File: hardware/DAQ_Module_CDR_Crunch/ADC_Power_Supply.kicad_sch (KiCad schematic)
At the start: 12 parts, among them U5 TPS70933DBVR, U6 TPS70933DBVR

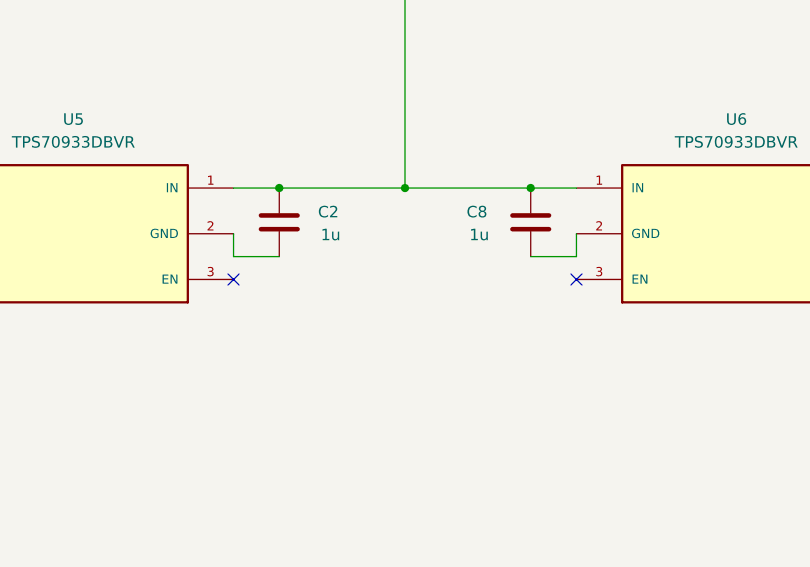
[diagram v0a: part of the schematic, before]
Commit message: Ready for final review. Added downloadable footprint and symbol of board
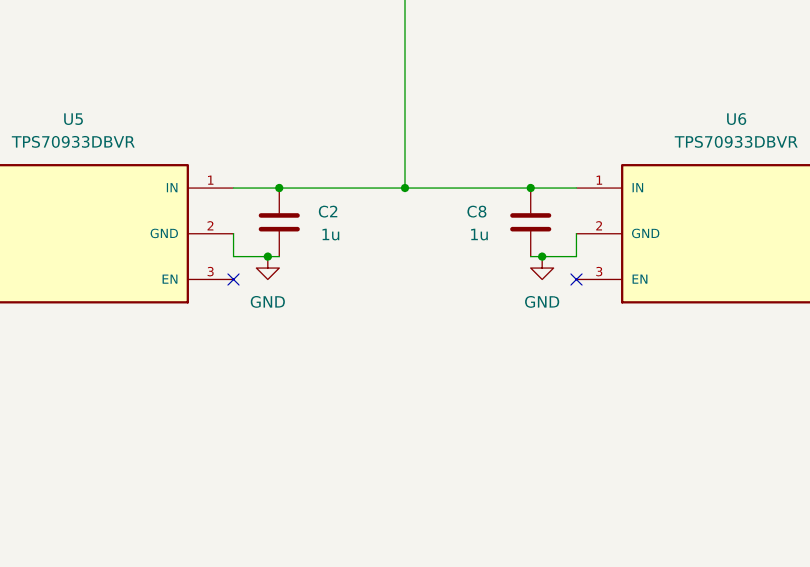
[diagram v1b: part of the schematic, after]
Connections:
- net GND: now also C2.1, C8.2, U5.2 (GND), U6.2 (GND)
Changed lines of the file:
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@@
+	)
+	(junction
+		(at 137.16 80.01)
+		(diameter 0)
+		(color 0 0 0 0)
 	)
 	(junction
@@
 	)
 	(junction
+		(at 106.68 80.01)
+		(diameter 0)
+		(color 0 0 0 0)
+	)
+	(junction
 		(at 195.58 105.41)
 		(diameter 0)
@@
 	(wire
 		(pts
-			(xy 107.95 80.01) (xy 102.87 80.01)
+			(xy 107.95 80.01) (xy 106.68 80.01)
 		)
 		(stroke
@@
 	(wire
 		(pts
-			(xy 135.89 80.01) (xy 140.97 80.01)
+			(xy 135.89 80.01) (xy 137.16 80.01)
+		)
+		(stroke
+			(width 0)
+			(type default)
+		)
+	)
+	(wire
+		(pts
+			(xy 106.68 80.01) (xy 102.87 80.01)
 		)
 		(stroke
@@
 		(pts
 			(xy 195.58 105.41) (xy 190.5 105.41)
+		)
+		(stroke
+			(width 0)
+			(type default)
+		)
+	)
+	(wire
+		(pts
+			(xy 137.16 80.01) (xy 140.97 80.01)
 		)
 		(stroke
@@
 				(path "/5227b8b5-3dda-44a0-8387-0a3150b59ce6/912d4027-c9f3-433b-9488-65ed5c4fb033"
 					(reference "#PWR010")
+					(unit 1)
+				)
+			)
+		)
+	)
+	(symbol
+		(lib_id "power:GND")
+		(at 106.68 80.01 0)
+		(unit 1)
+		(exclude_from_sim no)
+		(in_bom yes)
+		(on_board yes)
+		(dnp no)
+		(fields_autoplaced yes)
+		(property "Reference" "#PWR02"
+			(at 106.68 86.36 0)
+			(effects
+				(font
+					(size 1.27 1.27)
+				)
+				(hide yes)
+			)
+		)
+		(property "Value" "GND"
+			(at 106.68 85.09 0)
+			(effects
+				(font
+					(size 1.27 1.27)
+				)
+			)
+		)
+		(property "Footprint" ""
+			(at 106.68 80.01 0)
+			(effects
+				(font
+					(size 1.27 1.27)
+				)
+				(hide yes)
+			)
+		)
+		(property "Datasheet" ""
+			(at 106.68 80.01 0)
+			(effects
+				(font
+					(size 1.27 1.27)
+				)
+				(hide yes)
+			)
+		)
+		(property "Description" "Power symbol creates a global label with name \"GND\" , ground"
+			(at 106.68 80.01 0)
+			(effects
+				(font
+					(size 1.27 1.27)
+				)
+				(hide yes)
+			)
+		)
+		(pin "1"
+		)
+		(instances
+			(project ""
+				(path "/5227b8b5-3dda-44a0-8387-0a3150b59ce6/912d4027-c9f3-433b-9488-65ed5c4fb033"
+					(reference "#PWR02")
 					(unit 1)
 				)
@@
 					(unit 1)
 				)
+			)
+		)
+	)
+	(symbol
+		(lib_id "power:GND")
+		(at 137.16 80.01 0)
+		(unit 1)
+		(exclude_from_sim no)
+		(in_bom yes)
+		(on_board yes)
+		(dnp no)
+		(fields_autoplaced yes)
+		(property "Reference" "#PWR06"
+			(at 137.16 86.36 0)
+			(effects
+				(font
+					(size 1.27 1.27)
+				)
+				(hide yes)
+			)
+		)
+		(property "Value" "GND"
+			(at 137.16 85.09 0)
+			(effects
+				(font
+					(size 1.27 1.27)
+				)
+			)
+		)
+		(property "Footprint" ""
+			(at 137.16 80.01 0)
+			(effects
+				(font
+					(size 1.27 1.27)
+				)
+				(hide yes)
+			)
+		)
+		(property "Datasheet" ""
+			(at 137.16 80.01 0)
+			(effects
+				(font
+					(size 1.27 1.27)
+				)
+				(hide yes)
+			)
+		)
+		(property "Description" "Power symbol creates a global label with name \"GND\" , ground"
+			(at 137.16 80.01 0)
+			(effects
+				(font
+					(size 1.27 1.27)
+				)
+				(hide yes)
+			)
+		)
+		(pin "1"
+		)
+		(instances
+			(project ""
+				(path "/5227b8b5-3dda-44a0-8387-0a3150b59ce6/912d4027-c9f3-433b-9488-65ed5c4fb033"
+					(reference "#PWR06")
+					(unit 1)
+				)
